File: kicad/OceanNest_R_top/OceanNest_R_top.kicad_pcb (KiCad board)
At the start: 2 copper layers, 113.9 x 88.7 mm, 18 parts, among them SW21 SW_Push, SW22 SW_Push, SW23 SW_Push, SW24 SW_Push, SW25 SW_Push, SW26 SW_Push, SW27 SW_Push, SW28 SW_Push, SW29 SW_Push, SW30 SW_Push, SW31 SW_Push, SW32 SW_Push, SW33 SW_Push, SW34 SW_Push

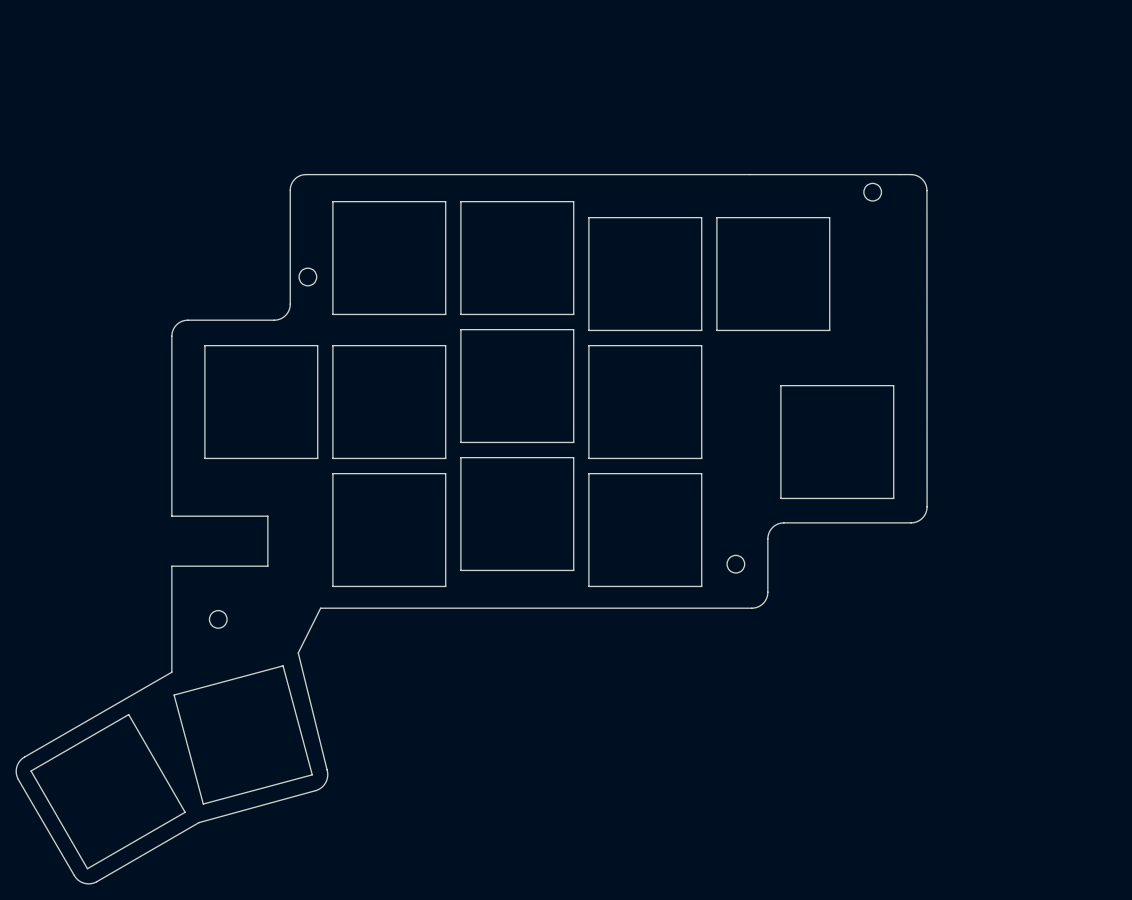
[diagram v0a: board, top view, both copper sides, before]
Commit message: Update right PCB layout and PMW3610 design notes
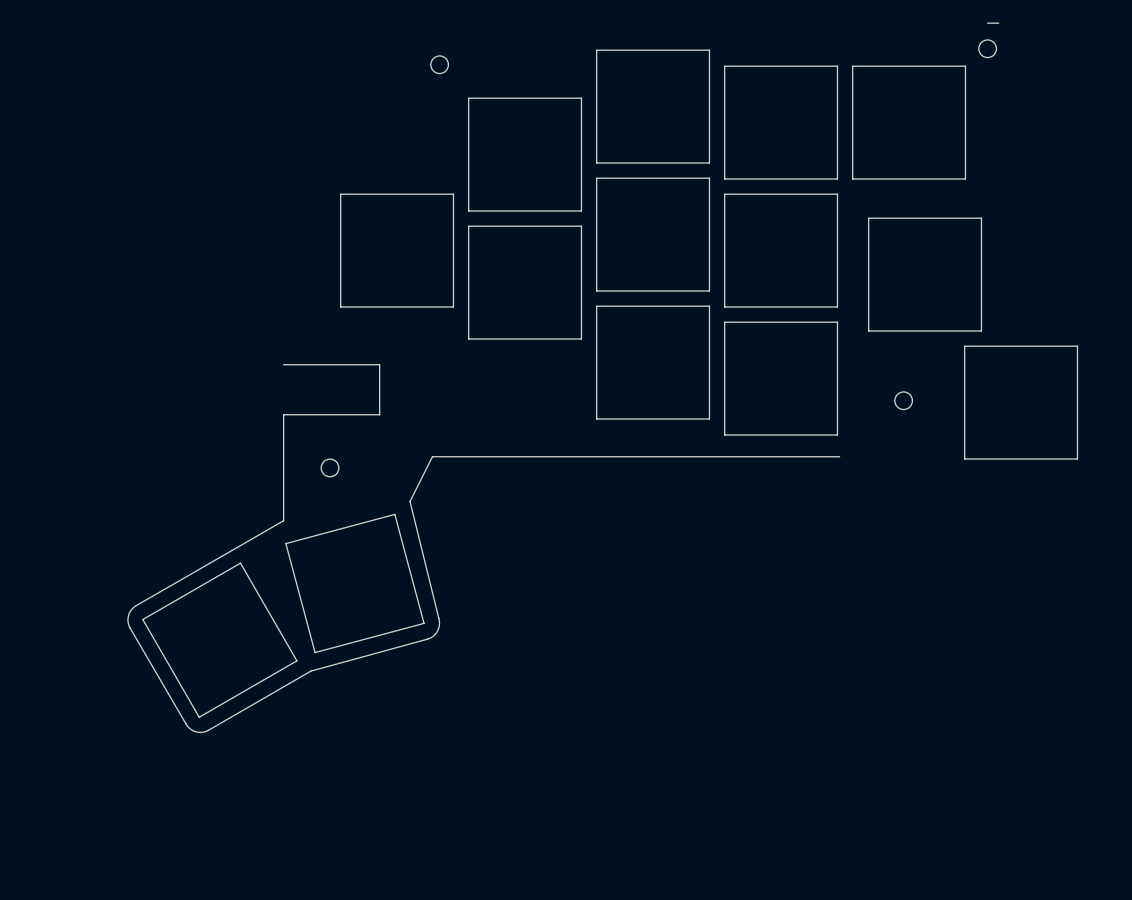
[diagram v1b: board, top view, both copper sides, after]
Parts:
- moved SW30 80.6 mm to (200.2, 90.3)
- moved hole2 31.2 mm to (127.5, 48.1)
- moved hole2 29.3 mm to (185.5, 90.1)
- moved SW25 25.4 mm to (122.2, 71.3)
- moved SW27 25.4 mm to (154.2, 69.3)
- moved SW28 25.4 mm to (170.2, 71.3)
- moved SW31 25.4 mm to (154.2, 85.3)
- moved SW32 25.4 mm to (170.2, 87.3)
- moved SW22 25.4 mm to (154.2, 53.3)
- moved SW23 25.4 mm to (170.2, 55.3)
- moved SW24 25.4 mm to (186.2, 55.3)
- moved SW29 23.6 mm to (188.2, 74.3)
- moved SW34 23.5 mm to (116.9, 112.9)
- moved hole1 23.5 mm to (113.8, 98.5)
- moved SW33 23.5 mm to (100.0, 120.0)
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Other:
- board size 113.9 x 88.7 mm -> 108.8 x 88.7 mm

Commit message: Refine top cover board outline
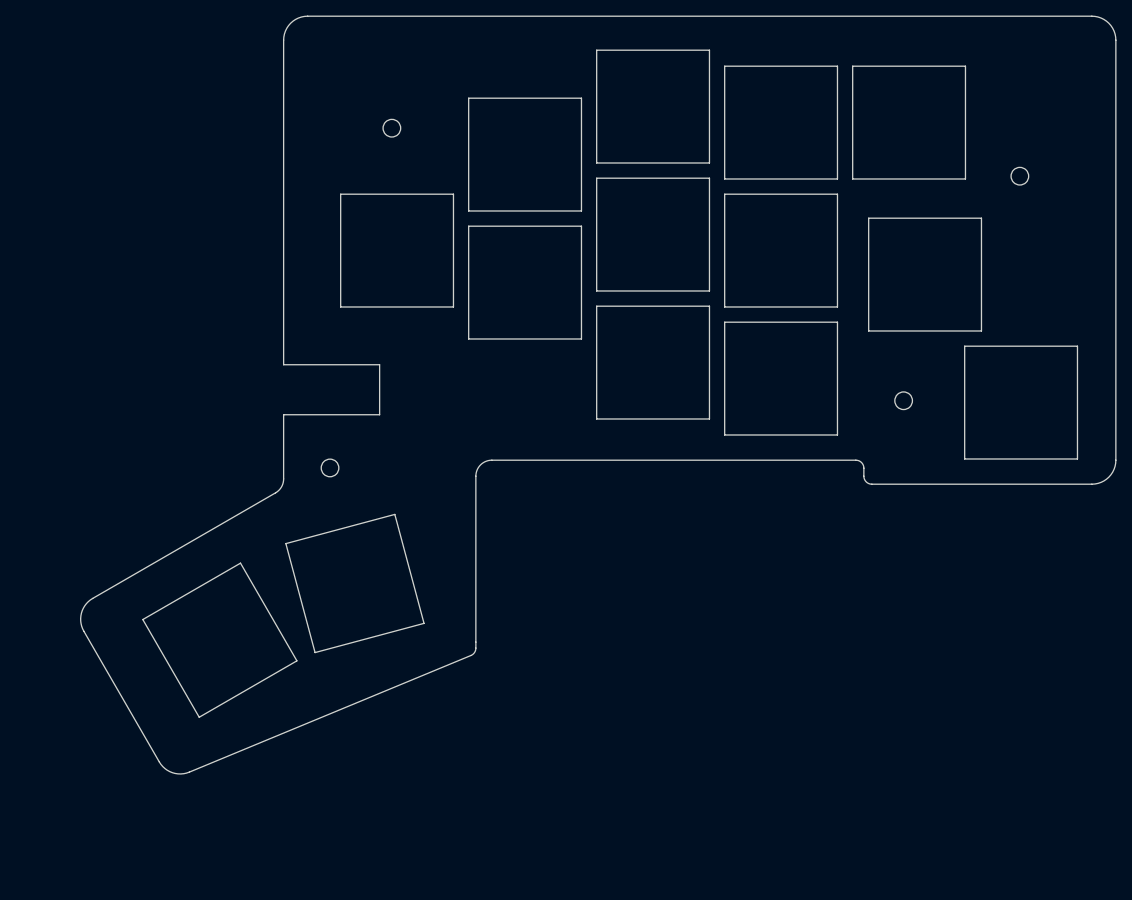
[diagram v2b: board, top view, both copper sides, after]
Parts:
- moved hole2 16.4 mm to (200.0, 62.0)
- moved hole2 9.93 mm to (121.5, 56.0)
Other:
- board size 108.8 x 88.7 mm -> 129.4 x 94.7 mm
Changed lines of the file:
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@@
 	(footprint "kbd_Hole:m2_Screw_Hole"
 		(layer "F.Cu")
-		(at 195.9703 46.0676)
+		(at 200 62)
 		(descr "Mounting Hole 2.2mm, no annular, M2")
 		(tags "mounting hole 2.2mm no annular m2")
@@
 	(footprint "kbd_Hole:m2_Screw_Hole"
 		(layer "F.Cu")
-		(at 127.4703 48.0676)
+		(at 121.5 56)
 		(descr "Mounting Hole 2.2mm, no annular, M2")
 		(tags "mounting hole 2.2mm no annular m2")
@@
 	)
 	(gr_arc
-		(start 88.770302 118.467601)
-		(mid 88.590402 116.901915)
-		(end 89.570302 115.667601)
+		(start 83 118.880711)
+		(mid 82.700294 116.604248)
+		(end 84.098076 114.782635)
 		(stroke
 			(width 0.05)
@@
 	)
 	(gr_line
-		(start 88.770302 118.467601)
-		(end 95.770302 130.467601)
+		(start 83 118.880711)
+		(end 92.434387 135.221548)
 		(stroke
 			(width 0.05)
@@
 	)
 	(gr_arc
-		(start 98.570302 131.267601)
-		(mid 97.004616 131.447501)
-		(end 95.770302 130.467601)
+		(start 96.180513 136.493187)
+		(mid 94.068158 136.562314)
+		(end 92.434387 135.221548)
 		(stroke
 			(width 0.05)
@@
 	)
 	(gr_line
-		(start 98.570302 131.267601)
-		(end 111.370302 123.867602)
+		(start 96.180513 136.493187)
+		(end 131.382683 121.911971)
+		(stroke
+			(width 0.05)
+			(type default)
+		)
+		(layer "Edge.Cuts")
+	)
+	(gr_line
+		(start 106.9703 101.57735)
+		(end 84.098076 114.782635)
+		(stroke
+			(width 0.05)
+			(type default)
+		)
+		(layer "Edge.Cuts")
+	)
+	(gr_arc
+		(start 107.9703 45)
+		(mid 108.84898 42.87868)
+		(end 110.9703 42)
+		(stroke
+			(width 0.05)
+			(type default)
+		)
+		(layer "Edge.Cuts")
+	)
+	(gr_line
+		(start 107.9703 85.5676)
+		(end 107.9703 45)
 		(stroke
 			(width 0.05)
@@
 	(gr_line
 		(start 107.9703 91.8176)
-		(end 107.9703 105.0676)
+		(end 107.9703 99.845299)
+		(stroke
+			(width 0.05)
+			(type default)
+		)
+		(layer "Edge.Cuts")
+	)
+	(gr_arc
+		(start 107.9703 99.845299)
+		(mid 107.702351 100.845299)
+		(end 106.9703 101.57735)
 		(stroke
 			(width 0.05)
@@
 	)
 	(gr_line
-		(start 107.970302 105.067601)
-		(end 89.570302 115.667601)
-		(stroke
-			(width 0.05)
-			(type solid)
-		)
-		(layer "Edge.Cuts")
-	)
-	(gr_line
-		(start 111.370302 123.867602)
-		(end 125.9703 119.867602)
+		(start 110.9703 42)
+		(end 209 42)
 		(stroke
 			(width 0.05)
@@
 	)
 	(gr_line
-		(start 123.7703 102.6676)
-		(end 126.5703 97.0676)
+		(start 132 99.5)
+		(end 132 120.239601)
+		(stroke
+			(width 0.05)
+			(type default)
+		)
+		(layer "Edge.Cuts")
+	)
+	(gr_arc
+		(start 132 99.5)
+		(mid 132.585786 98.085786)
+		(end 134 97.5)
+		(stroke
+			(width 0.05)
+			(type default)
+		)
+		(layer "Edge.Cuts")
+	)
+	(gr_arc
+		(start 132 120.988091)
+		(mid 131.831473 121.543665)
+		(end 131.382683 121.911971)
 		(stroke
 			(width 0.05)
@@
 	)
 	(gr_line
-		(start 126.5703 97.0676)
-		(end 177.4703 97.0676)
+		(start 132 120.988091)
+		(end 132 120.239601)
 		(stroke
 			(width 0.05)
@@
 	)
 	(gr_line
-		(start 127.3703 117.267602)
-		(end 123.7703 102.6676)
+		(start 179.5 97.5)
+		(end 134 97.5)
 		(stroke
 			(width 0.05)
@@
 	)
 	(gr_arc
-		(start 127.3703 117.267602)
-		(mid 127.208777 118.85755)
-		(end 125.9703 119.867602)
+		(start 179.5 97.5)
+		(mid 180.207107 97.792893)
+		(end 180.5 98.5)
 		(stroke
 			(width 0.05)
@@
 	)
 	(gr_line
-		(start 195.9703 42.8676)
-		(end 197.356086 42.8676)
-		(stroke
-			(width 0.05)
+		(start 180.5 99.5)
+		(end 180.5 98.5)
+		(stroke
+			(width 0.05)
+			(type default)
+		)
+		(layer "Edge.Cuts")
+	)
+	(gr_arc
+		(start 181.5 100.5)
+		(mid 180.792893 100.207107)
+		(end 180.5 99.5)
+		(stroke
+			(width 0.05)
+			(type default)
+		)
+		(layer "Edge.Cuts")
+	)
+	(gr_arc
+		(start 209 42)
+		(mid 211.12132 42.87868)
+		(end 212 45)
+		(stroke
+			(width 0.05)
+			(type default)
+		)
+		(layer "Edge.Cuts")
+	)
+	(gr_line
+		(start 209 100.5)
+		(end 181.5 100.5)
+		(stroke
+			(width 0.05)
+			(type default)
+		)
+		(layer "Edge.Cuts")
+	)
+	(gr_line
+		(start 212 45)
+		(end 212 97.5)
+		(stroke
+			(width 0.05)
+			(type default)
+		)
+		(layer "Edge.Cuts")
+	)
+	(gr_arc
+		(start 212 97.5)
+		(mid 211.12132 99.62132)
+		(end 209 100.5)
+		(stroke
+			(width 0.05)

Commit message: Adjust right top cover board geometry
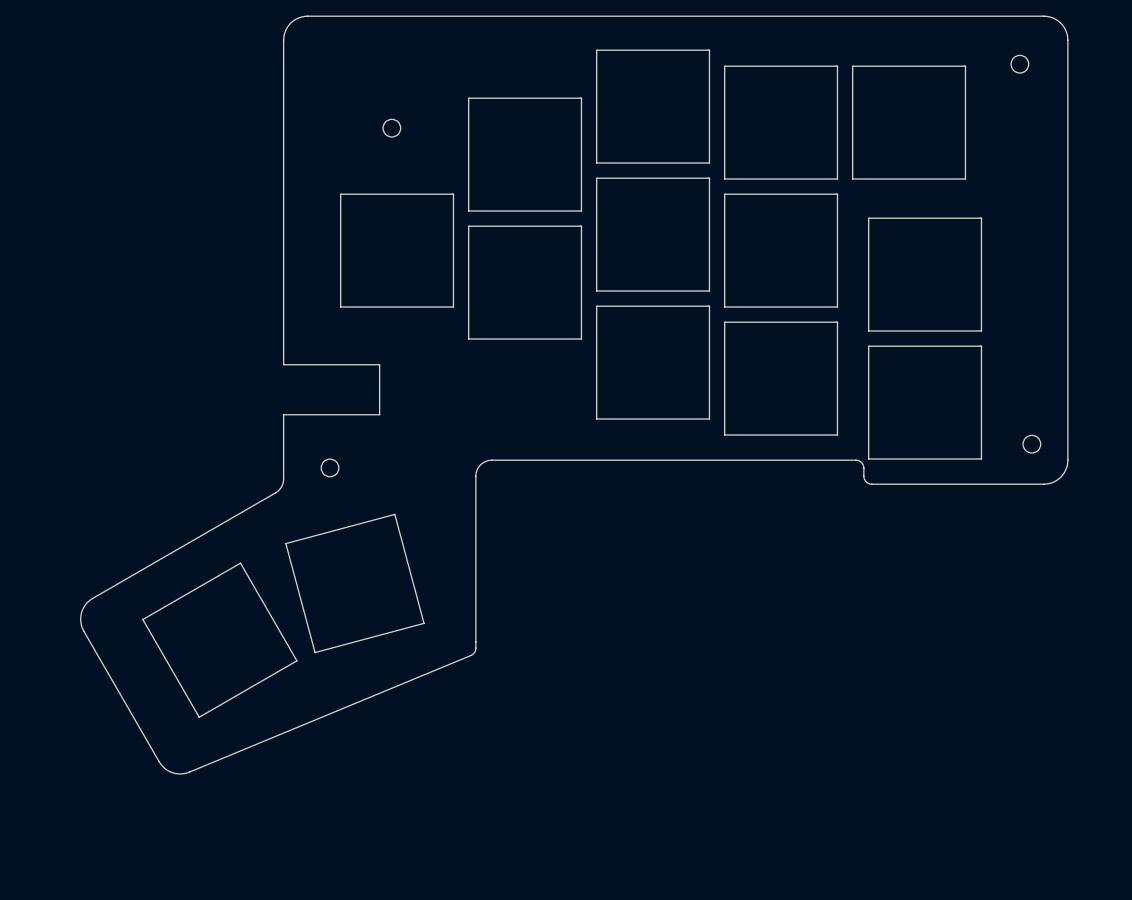
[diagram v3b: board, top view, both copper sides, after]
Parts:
- moved hole2 16.9 mm to (201.5, 95.5)
- moved hole2 14.0 mm to (200.0, 48.0)
- moved SW30 12.0 mm to (188.2, 90.3)
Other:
- board size 129.4 x 94.7 mm -> 123.4 x 94.7 mm
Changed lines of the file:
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@@
 	(footprint "kbd_Hole:m2_Screw_Hole"
 		(layer "F.Cu")
-		(at 185.4703 90.0676)
+		(at 201.5 95.5)
 		(descr "Mounting Hole 2.2mm, no annular, M2")
 		(tags "mounting hole 2.2mm no annular m2")
@@
 	(footprint "kbd_Hole:m2_Screw_Hole"
 		(layer "F.Cu")
-		(at 200 62)
+		(at 200 48)
 		(descr "Mounting Hole 2.2mm, no annular, M2")
 		(tags "mounting hole 2.2mm no annular m2")
@@
 	(footprint "isw-kbd:SW_Hole_CherryMX_16mm"
 		(layer "F.Cu")
-		(at 200.1503 90.2991)
+		(at 188.1503 90.2991)
 		(property "Reference" "SW30"
 			(at 4.4 2.5 0)
@@
 	(gr_line
 		(start 110.9703 42)
-		(end 209 42)
+		(end 203 42)
 		(stroke
 			(width 0.05)
@@
 	)
 	(gr_arc
-		(start 209 42)
-		(mid 211.12132 42.87868)
-		(end 212 45)
+		(start 203 42)
+		(mid 205.12132 42.87868)
+		(end 206 45)
 		(stroke
 			(width 0.05)
@@
 	)
 	(gr_line
-		(start 209 100.5)
+		(start 203 100.5)
 		(end 181.5 100.5)
 		(stroke
@@
 	)
 	(gr_line
-		(start 212 45)
-		(end 212 97.5)
+		(start 206 45)
+		(end 206 97.5)
 		(stroke
 			(width 0.05)
@@
 	)
 	(gr_arc
-		(start 212 97.5)
-		(mid 211.12132 99.62132)
-		(end 209 100.5)
+		(start 206 97.5)
+		(mid 205.12132 99.62132)
+		(end 203 100.5)
 		(stroke
 			(width 0.05)

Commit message: prepare outline
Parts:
- moved hole2 8.73 mm to (123.5, 47.5)
- moved hole1 7.57 mm to (115.0, 91.0)
- moved SW33 3.00 mm to (97.0, 120.0)
- moved SW34 3.00 mm to (113.9, 112.9)
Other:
- board size 123.4 x 94.7 mm -> 126.4 x 94.7 mm
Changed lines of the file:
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@@
 	(footprint "isw-kbd:SW_Hole_CherryMX_16mm"
 		(layer "F.Cu")
-		(at 100 120 30)
+		(at 97 120 30)
 		(property "Reference" "SW33"
 			(at 4.4 2.500001 30)
@@
 	(footprint "isw-kbd:SW_Hole_CherryMX_16mm"
 		(layer "F.Cu")
-		(at 116.8849 112.9125 15)
+		(at 113.8849 112.9125 15)
 		(property "Reference" "SW34"
 			(at 4.4 2.5 15)
@@
 	(footprint "kbd_Hole:m2_Screw_Hole"
 		(layer "F.Cu")
-		(at 121.5 56)
+		(at 123.5 47.5)
 		(descr "Mounting Hole 2.2mm, no annular, M2")
 		(tags "mounting hole 2.2mm no annular m2")
@@
 	(footprint "kbd_Hole:m2_Screw_Hole"
 		(layer "F.Cu")
-		(at 113.7703 98.4676)
+		(at 115 91)
 		(descr "Mounting Hole 2.2mm, no annular, M2")
 		(tags "mounting hole 2.2mm no annular m2")
@@
 	)
 	(gr_arc
-		(start 83 118.880711)
-		(mid 82.700294 116.604248)
-		(end 84.098076 114.782635)
+		(start 80 118.880711)
+		(mid 79.700294 116.604248)
+		(end 81.098076 114.782635)
 		(stroke
 			(width 0.05)
@@
 	)
 	(gr_line
-		(start 83 118.880711)
-		(end 92.434387 135.221548)
+		(start 80 118.880711)
+		(end 89.434387 135.221548)
 		(stroke
 			(width 0.05)
@@
 	)
 	(gr_arc
-		(start 96.180513 136.493187)
-		(mid 94.068158 136.562314)
-		(end 92.434387 135.221548)
+		(start 93.180513 136.493187)
+		(mid 91.068158 136.562314)
+		(end 89.434387 135.221548)
 		(stroke
 			(width 0.05)
@@
 	)
 	(gr_line
-		(start 96.180513 136.493187)
-		(end 131.382683 121.911971)
+		(start 93.180513 136.493187)
+		(end 128.382683 121.911971)
 		(stroke
 			(width 0.05)
@@
 	)
 	(gr_line
-		(start 106.9703 101.57735)
-		(end 84.098076 114.782635)
+		(start 103.9703 101.57735)
+		(end 81.098076 114.782635)
 		(stroke
 			(width 0.05)
@@
 		(layer "Edge.Cuts")
 	)
-	(gr_arc
-		(start 107.9703 45)
-		(mid 108.84898 42.87868)
-		(end 110.9703 42)
+	(gr_line
+		(start 104.9703 45)
+		(end 104.9703 50.5676)
 		(stroke
 			(width 0.05)
@@
 		(layer "Edge.Cuts")
 	)
-	(gr_line
-		(start 107.9703 85.5676)
-		(end 107.9703 45)
+	(gr_arc
+		(start 104.9703 45)
+		(mid 105.84898 42.87868)
+		(end 107.9703 42)
 		(stroke
 			(width 0.05)
@@
 	)
 	(gr_line
-		(start 107.9703 85.5676)
-		(end 119.9703 85.5676)
+		(start 104.9703 50.5676)
+		(end 116.9703 50.5676)
 		(stroke
 			(width 0.05)
@@
 	)
 	(gr_line
-		(start 107.9703 91.8176)
-		(end 107.9703 99.845299)
+		(start 104.9703 56.8176)
+		(end 104.9703 99.845299)
 		(stroke
 			(width 0.05)
@@
 	)
 	(gr_arc
-		(start 107.9703 99.845299)
-		(mid 107.702351 100.845299)
-		(end 106.9703 101.57735)
+		(start 104.9703 99.845299)
+		(mid 104.702351 100.845299)
+		(end 103.9703 101.57735)
 		(stroke
 			(width 0.05)
@@
 	)
 	(gr_line
-		(start 110.9703 42)
+		(start 107.9703 42)
 		(end 203 42)
 		(stroke
@@
 	)
 	(gr_line
-		(start 119.9703 85.5676)
-		(end 119.9703 91.8176)
+		(start 116.9703 50.5676)
+		(end 116.9703 56.8176)
 		(stroke
 			(width 0.05)
@@
 	)
 	(gr_line
-		(start 119.9703 91.8176)
-		(end 107.9703 91.8176)
+		(start 116.9703 56.8176)
+		(end 104.9703 56.8176)
 		(stroke
 			(width 0.05)
@@
 	)
 	(gr_line
-		(start 132 99.5)
-		(end 132 120.239601)
+		(start 129 99.5)
+		(end 129 120.239601)
 		(stroke
 			(width 0.05)
@@
 	)
 	(gr_arc
-		(start 132 99.5)
-		(mid 132.585786 98.085786)
-		(end 134 97.5)
+		(start 129 99.5)
+		(mid 129.585786 98.085786)
+		(end 131 97.5)
 		(stroke
 			(width 0.05)
@@
 	)
 	(gr_arc
-		(start 132 120.988091)
-		(mid 131.831473 121.543665)
-		(end 131.382683 121.911971)
+		(start 129 120.988091)
+		(mid 128.831473 121.543665)
+		(end 128.382683 121.911971)
 		(stroke
 			(width 0.05)
@@
 	)
 	(gr_line
-		(start 132 120.988091)
-		(end 132 120.239601)
+		(start 129 120.988091)
+		(end 129 120.239601)
 		(stroke
 			(width 0.05)
@@
 	)
 	(gr_line
-		(start 179.5 97.5)
-		(end 134 97.5)
+		(start 176.5 97.5)
+		(end 131 97.5)
 		(stroke
 			(width 0.05)
@@
 	)
 	(gr_arc
-		(start 179.5 97.5)
-		(mid 180.207107 97.792893)
-		(end 180.5 98.5)
+		(start 176.5 97.5)
+		(mid 177.207107 97.792893)
+		(end 177.5 98.5)
 		(stroke
 			(width 0.05)
@@
 	)
 	(gr_line
-		(start 180.5 99.5)
-		(end 180.5 98.5)
+		(start 177.5 99.5)
+		(end 177.5 98.5)
 		(stroke
 			(width 0.05)
@@
 	)
 	(gr_arc
-		(start 181.5 100.5)
-		(mid 180.792893 100.207107)
-		(end 180.5 99.5)
+		(start 178.5 100.5)
+		(mid 177.792893 100.207107)
+		(end 177.5 99.5)
 		(stroke
 			(width 0.05)
@@
 	(gr_line
 		(start 203 100.5)
-		(end 181.5 100.5)
+		(end 178.5 100.5)
 		(stroke
 			(width 0.05)

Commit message: routing
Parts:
- moved hole1 4.00 mm to (115.0, 95.0)
- moved hole2 1.58 mm to (200.0, 95.0)
- moved hole2 0.71 mm to (123.0, 48.0)
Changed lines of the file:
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@@
 	(footprint "kbd_Hole:m2_Screw_Hole"
 		(layer "F.Cu")
-		(at 201.5 95.5)
+		(at 200 95)
 		(descr "Mounting Hole 2.2mm, no annular, M2")
 		(tags "mounting hole 2.2mm no annular m2")
@@
 	(footprint "kbd_Hole:m2_Screw_Hole"
 		(layer "F.Cu")
-		(at 123.5 47.5)
+		(at 123 48)
 		(descr "Mounting Hole 2.2mm, no annular, M2")
 		(tags "mounting hole 2.2mm no annular m2")
@@
 	(footprint "kbd_Hole:m2_Screw_Hole"
 		(layer "F.Cu")
-		(at 115 91)
+		(at 115 95)
 		(descr "Mounting Hole 2.2mm, no annular, M2")
 		(tags "mounting hole 2.2mm no annular m2")
